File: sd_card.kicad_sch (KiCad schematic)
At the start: 12 parts, among them J1101 DM3AT-SF-PEJM5

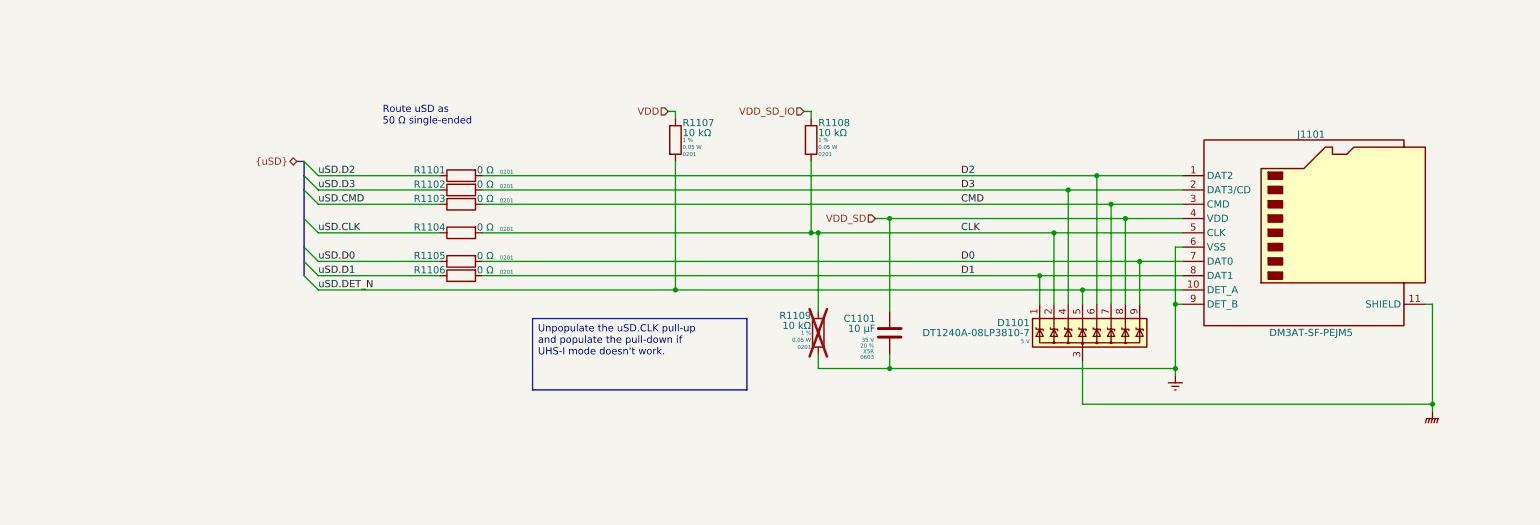
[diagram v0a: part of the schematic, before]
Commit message: Reorganize schematics
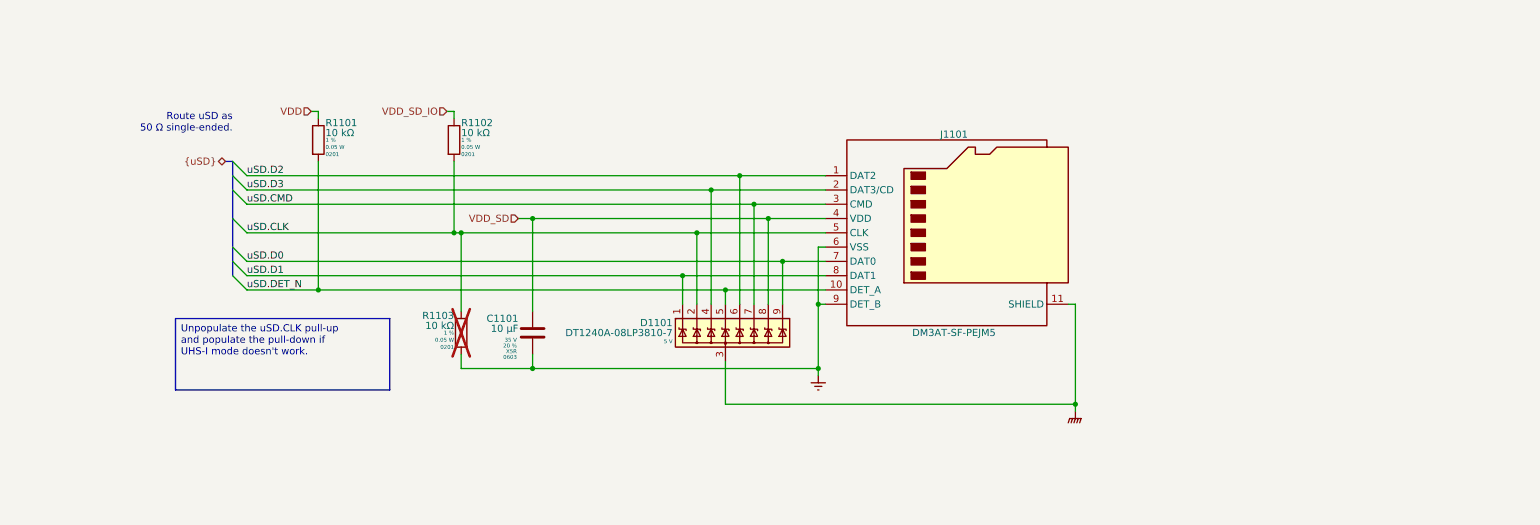
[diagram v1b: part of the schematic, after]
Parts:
- removed R1101, R1102, R1103, R1104, R1105, R1106: 0 Ω, perfect_footprints:R_0201_0603Metric, symbol Device:R
- renumbered R1107 to R1101, R1108 to R1102, R1109 to R1103
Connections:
- net CLK is gone; now on net uSD.CLK: D1101.2 (Line-3), J1101.5 (CLK), R1102.2, R1103.1
- net CMD is gone; now on net uSD.CMD: D1101.7 (Line-5), J1101.3 (CMD)
- net D0 is gone; now on net uSD.D0: D1101.9 (Line-2), J1101.7 (DAT0)
- net D1 is gone; now on net uSD.D1: D1101.1 (Line-1), J1101.8 (DAT1)
- net D2 is gone; now on net uSD.D2: D1101.6 (Line-7), J1101.1 (DAT2)
- net D3 is gone; now on net uSD.D3: D1101.4 (Line-6), J1101.2 (DAT3/CD)
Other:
- note added: "Route uSD as 50 Ω single-ended."
- note removed: "Route uSD as 50 Ω single-ended"
- moved on the sheet: C1101, D1101, J1101, R1101, R1102, R1103

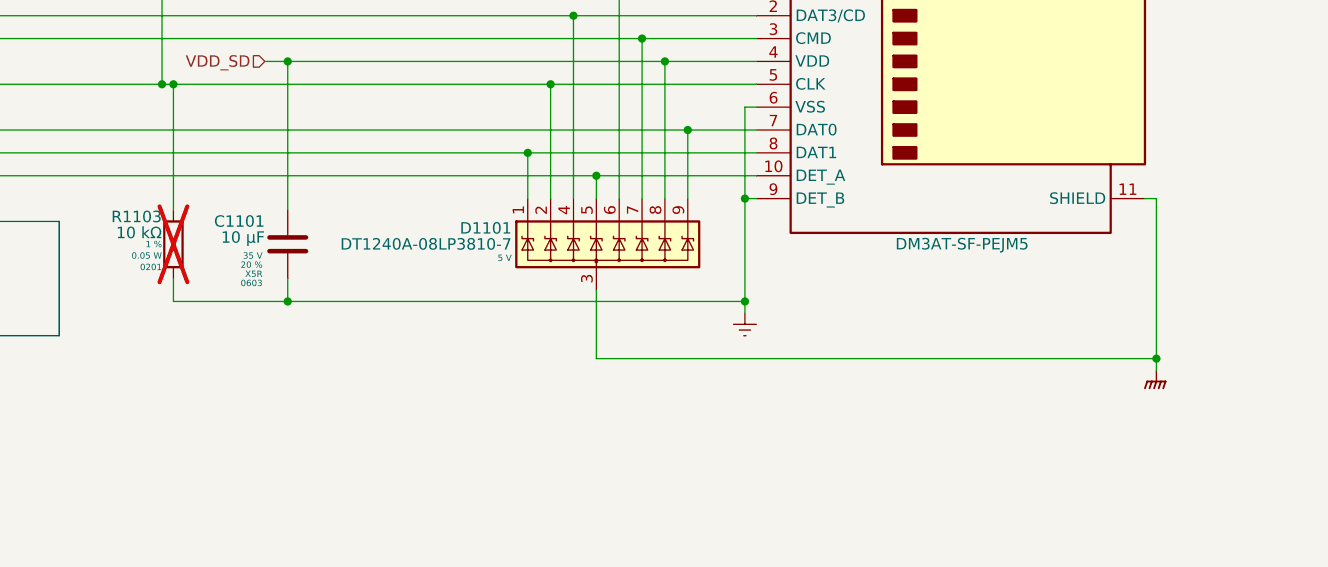
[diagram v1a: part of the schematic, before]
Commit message: Update schematics to Kicad 10
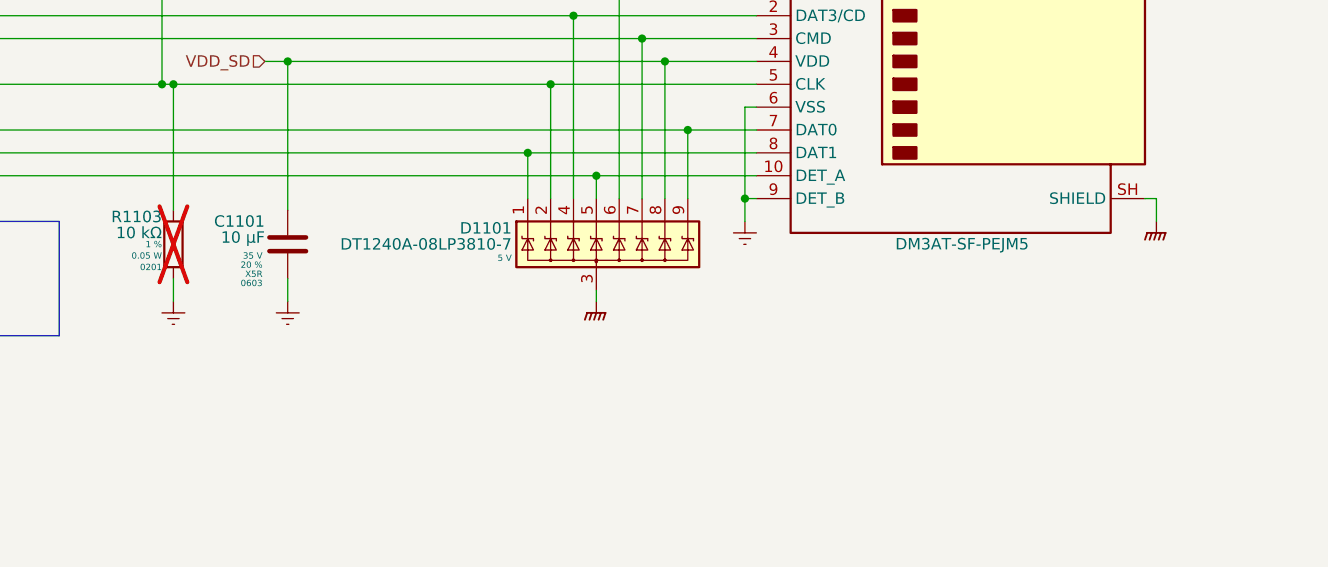
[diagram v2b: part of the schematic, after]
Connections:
- net CHASSIS: now also J1101.SH (SHIELD); no longer J1101.11 (SHIELD)
